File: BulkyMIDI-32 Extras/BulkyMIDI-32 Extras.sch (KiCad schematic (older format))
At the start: 64 parts, among them J1 DC IN, J10 MIDI2, J11 MIDI3, J12 SERIAL, J13 ICSP, J14 BIN/ASCII, J15 BAUD_RATE, J16 Stacked RS232 Module, J2 MIDI OUT, J3 MIDI IN, J4 Conn_Extras, J5 MIDI1, J6 RS232 Module, J7 INPUT1, J8 INPUT2, J9 OUTPUT, M1 Mounting, M2 Mounting, M3 Mounting, M4 Mounting, SW1 RESET, U1 74HCT14, U2 ATMEGA328_MCU, U3 6N138, Y1 16Mhz

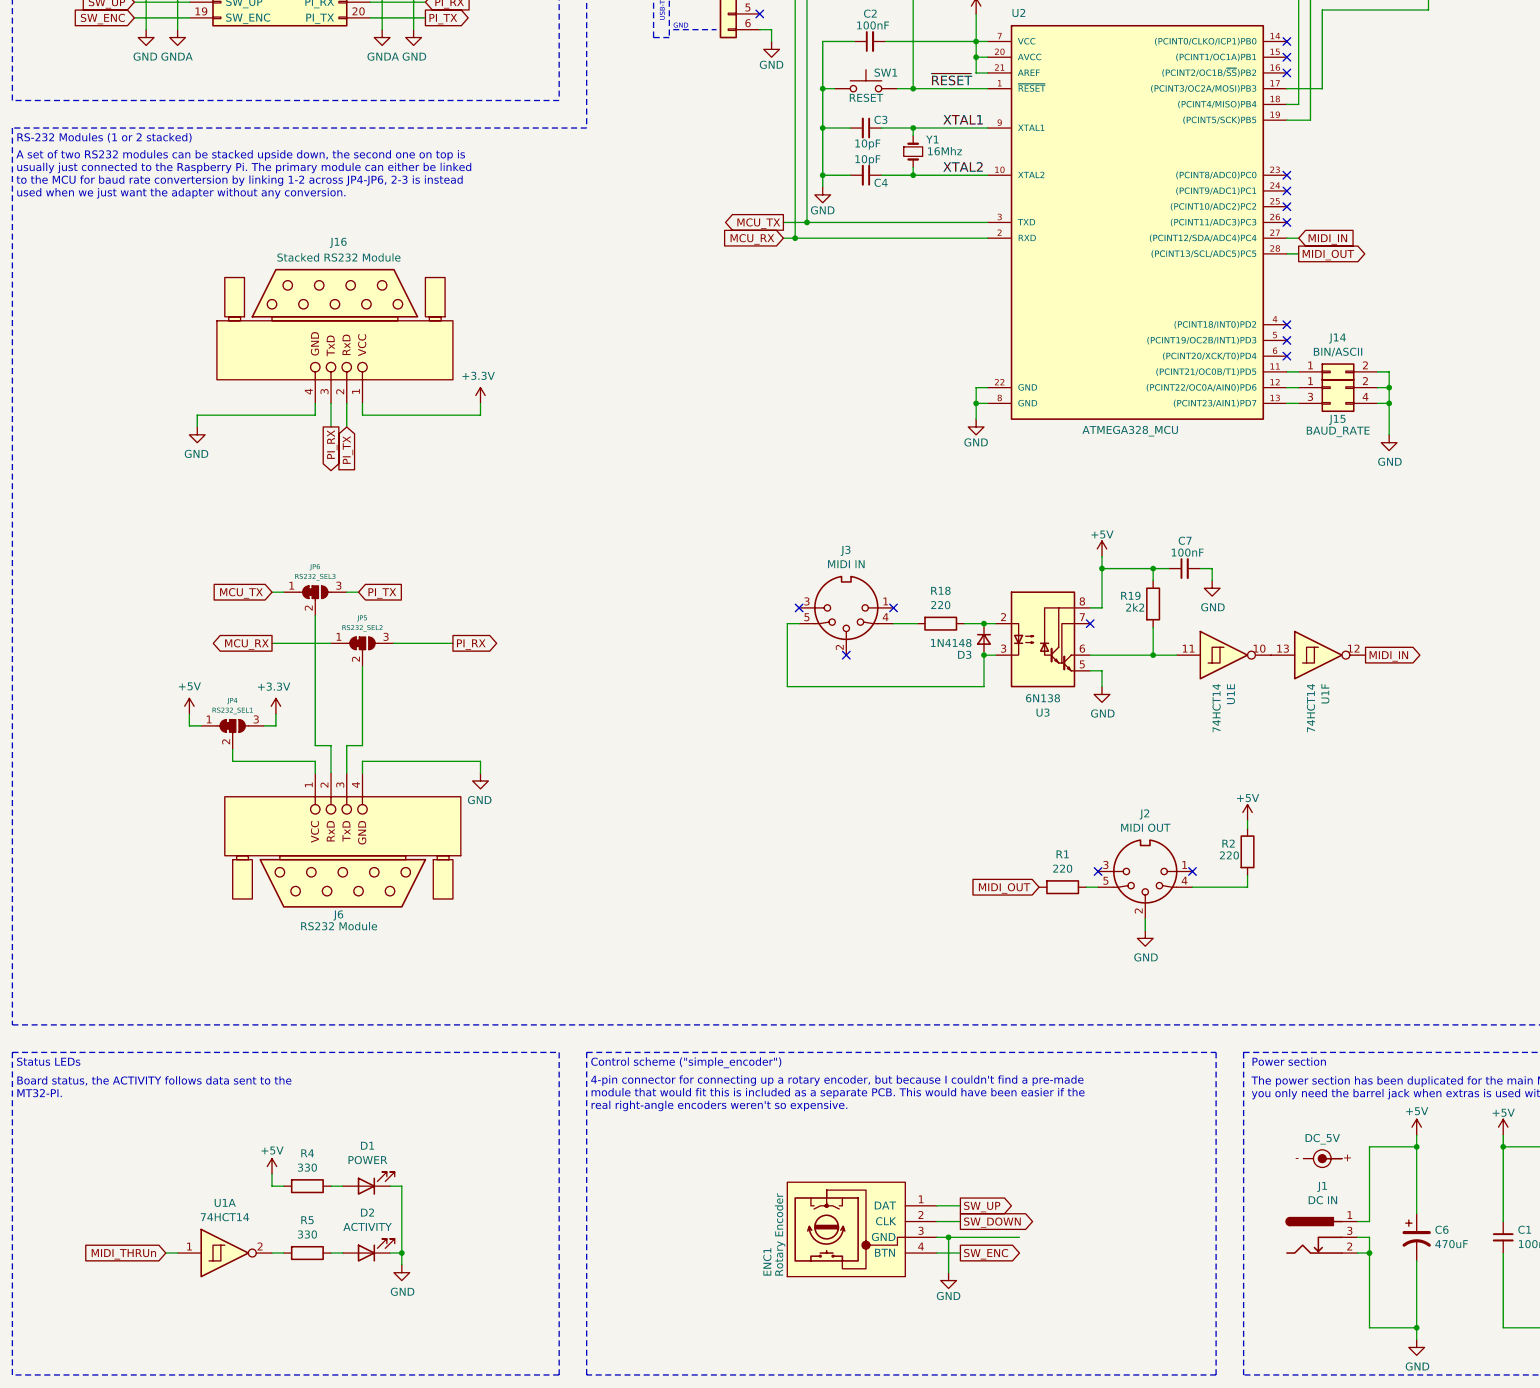
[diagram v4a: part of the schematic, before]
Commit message: Add third status LED
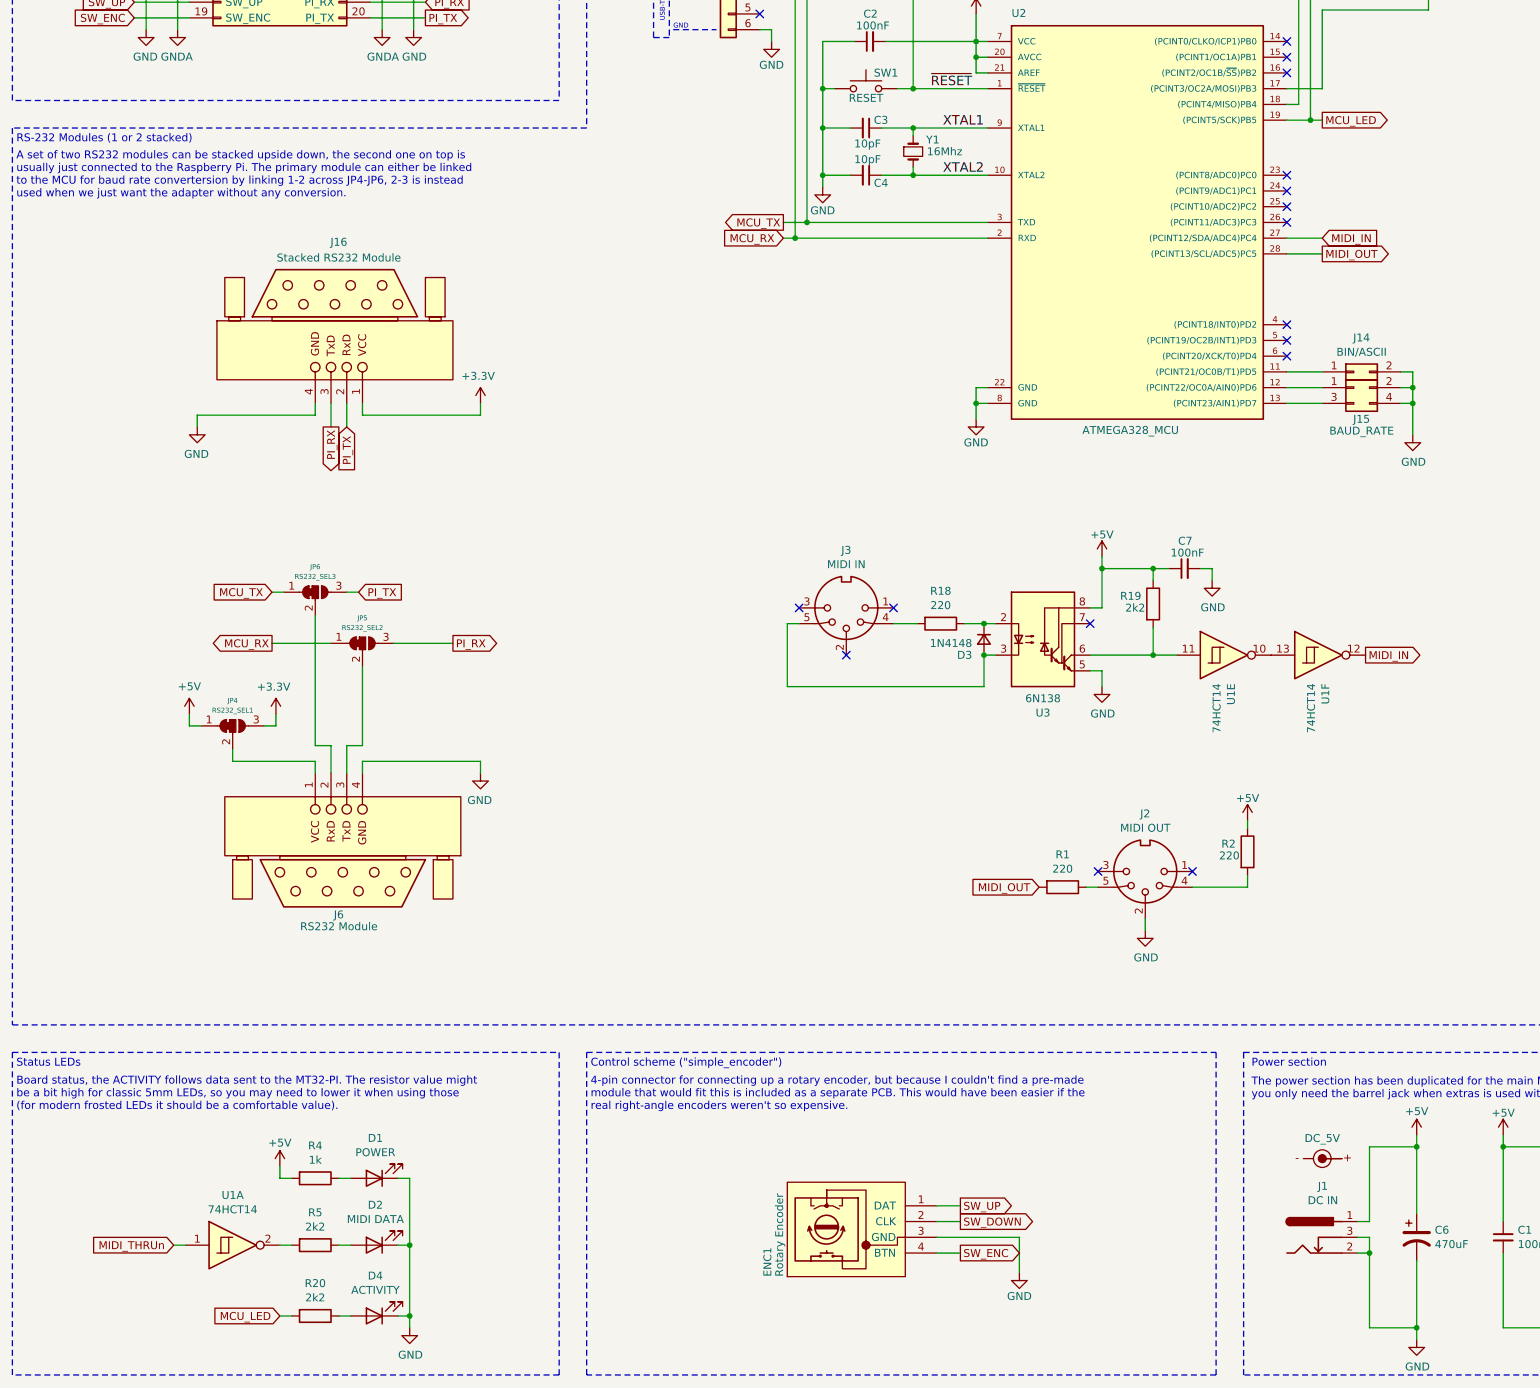
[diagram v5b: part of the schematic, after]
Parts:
- added D4: ACTIVITY, LED_THT:LED_D5.0mm_Horizontal_O1.27mm_Z3.0mm, symbol Device:LED
- added R20: 2k2, Resistor_THT:R_Axial_DIN0207_L6.3mm_D2.5mm_P10.16mm_Horizontal, symbol Device:R
- D2: value ACTIVITY -> MIDI DATA
- R4: value 330 -> 1k
- R5: value 330 -> 2k2
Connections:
- net GND: now also D4.1 (K)
- net MCU_LED: now reaches J13.3 (Pin_3), U2.19 ((PCINT5/SCK)PB5)
- net MCU_LED: now also R20.2
- new net: D4.2 (A), R20.1
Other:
- note added: "Board status, the ACTIVITY follows data sent to the MT32-PI. The resistor value might\nbe a bit high for classic 5mm LEDs, so you may need to lower it when using those\n(for modern frosted LEDs it should be a comfortable value)."
- note removed: "Board status, the ACTIVITY follows data sent to the\nMT32-PI."
- moved on the sheet: D1, D2, J14, J15, R4, R5, U1A

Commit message: Better LED naming
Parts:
- D2: value MIDI DATA -> DATA (MT-32)
- D4: value ACTIVITY -> ACTIVITY (MCU)
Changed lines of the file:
@@
 P 3300 10300
 F 0 "D2" H 3293 10045 50  0000 C CNN
-F 1 "MIDI DATA" H 3293 10136 50  0000 C CNN
+F 1 "DATA (MT-32)" H 3293 10136 50  0000 C CNN
 F 2 "LED_THT:LED_D5.0mm_Horizontal_O1.27mm_Z3.0mm" H 3300 10300 50  0001 C CNN
 F 3 "~" H 3300 10300 50  0001 C CNN
@@
 P 3300 10750
 F 0 "D4" H 3293 10495 50  0000 C CNN
-F 1 "ACTIVITY" H 3293 10586 50  0000 C CNN
+F 1 "ACTIVITY (MCU)" H 3293 10586 50  0000 C CNN
 F 2 "LED_THT:LED_D5.0mm_Horizontal_O1.27mm_Z3.0mm" H 3300 10750 50  0001 C CNN
 F 3 "~" H 3300 10750 50  0001 C CNN

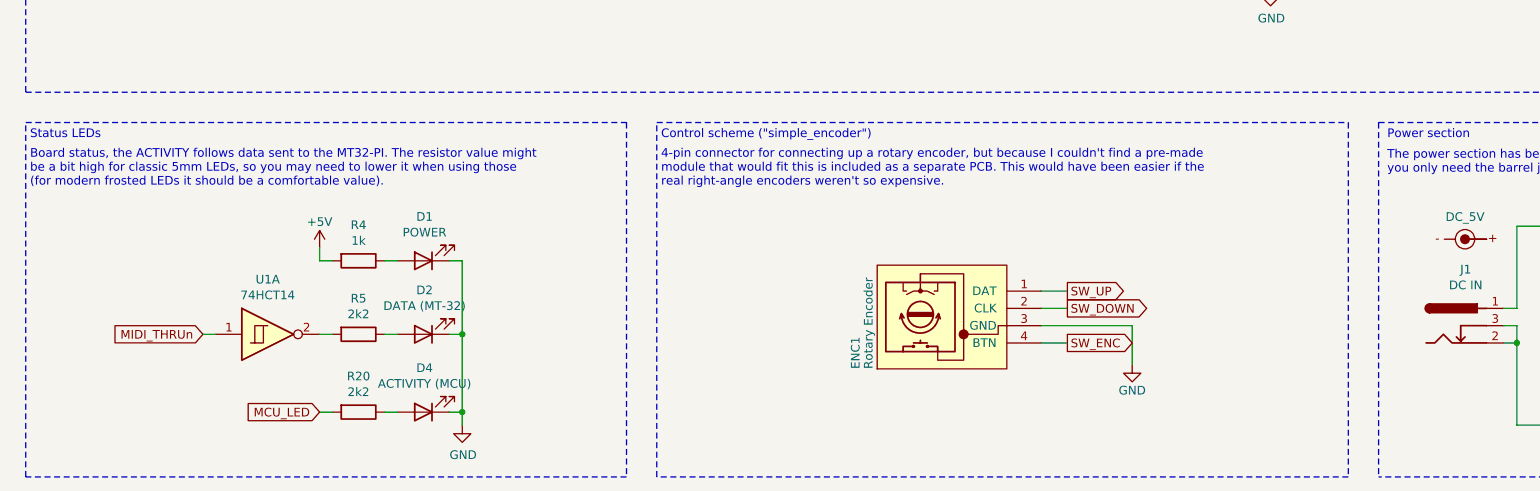
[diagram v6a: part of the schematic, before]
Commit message: Made DATA LED a bit nicer, moved rotary encoder slightly
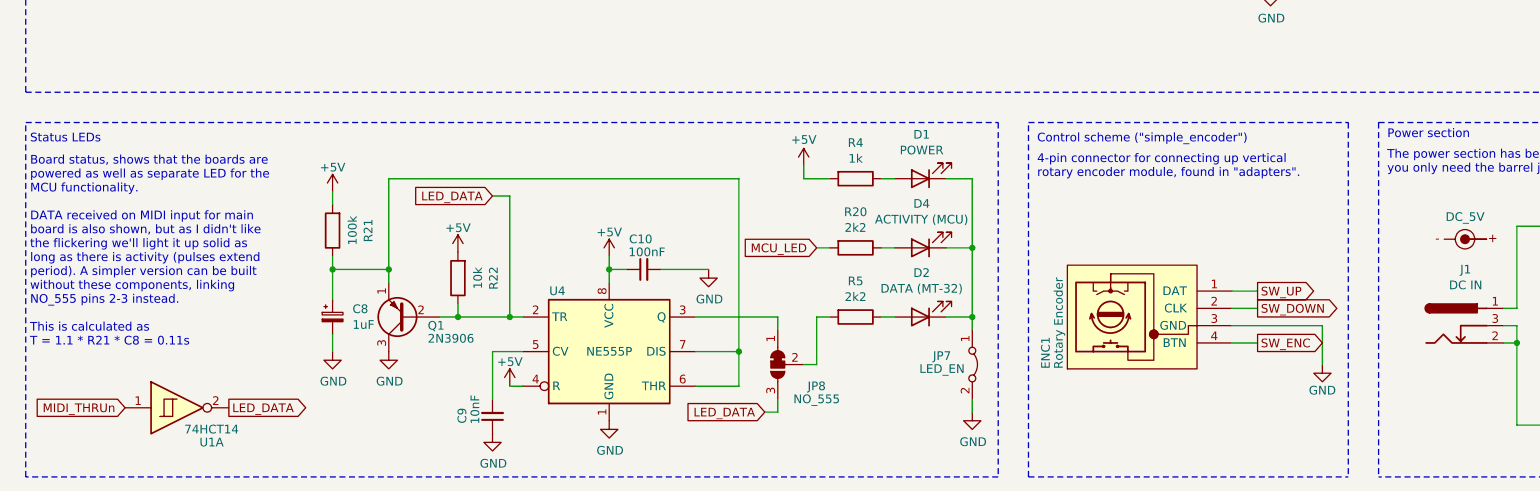
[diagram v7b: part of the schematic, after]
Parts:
- added C10: 100nF, Capacitor_THT:C_Disc_D4.7mm_W2.5mm_P5.00mm, symbol Device:C_Small
- added C8: 1uF, Capacitor_THT:CP_Radial_D5.0mm_P2.00mm, symbol Device:CP_Small
- added C9: 10nF, Capacitor_THT:C_Disc_D4.7mm_W2.5mm_P5.00mm, symbol Device:C_Small
- added JP7: LED_EN, Connector_PinHeader_2.54mm:PinHeader_1x02_P2.54mm_Vertical, symbol Jumper:Jumper_2_Bridged
- added JP8: NO_555, Jumper:SolderJumper-3_P1.3mm_Open_Pad1.0x1.5mm, symbol Jumper:SolderJumper_3_Bridged12
- added Q1: 2N3906, Package_TO_SOT_THT:TO-92_Inline_Wide, symbol Transistor_BJT:2N3906
- added R21: 100k, Resistor_THT:R_Axial_DIN0207_L6.3mm_D2.5mm_P10.16mm_Horizontal, symbol Device:R
- added R22: 10k, Resistor_THT:R_Axial_DIN0207_L6.3mm_D2.5mm_P10.16mm_Horizontal, symbol Device:R
- added U4: NE555P, Package_DIP:DIP-8_W7.62mm_Socket_LongPads, symbol Timer:NE555P
- SW1: footprint Button_Switch_THT:SW_PUSH_6mm -> Button_Switch_THT:SW_Tactile_SPST_Angled_PTS645Vx39-2LFS
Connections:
- net +5V: now also C10.1, R21.2, R22.2, U4.4 (R), U4.8 (VCC)
- net GND: now also C10.2, C8.2, C9.1, JP7.2 (B), Q1.3 (C), U4.1 (GND); no longer D1.1 (K), D2.1 (K), D4.1 (K)
- net at R5.2: now also JP8.2 (C); no longer U1.2
- new net: D1.1 (K), D2.1 (K), D4.1 (K), JP7.1 (A)
- new net: JP8.1 (A), U4.3 (Q)
- new net: C9.2, U4.5 (CV)
- new net: C8.1, Q1.1 (E), R21.1, U4.6 (THR), U4.7 (DIS)
- new net LED_DATA: JP8.3 (B), Q1.2 (B), R22.1, U1.2, U4.2 (TR)
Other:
- note added: "4-pin connector for connecting up vertical\nrotary encoder module, found in "adapters"."
- note added: "Board status, shows that the boards are\npowered as well as separate LED for the\nMCU functionality.\n\nDATA received on MIDI input for main\nboard is also shown, but as I didn't like\nthe flickering we'll light it up solid as\nlong as there is activity (pulses extend\nperiod). A simpler version can be built\nwithout these components, linking\nNO_555 pins 2-3 instead.\n\nThis is calculated as\nT 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"
- note removed: "4-pin connector for connecting up a rotary encoder, but because I couldn't find a pre-made\nmodule that would fit this is included as a separate PCB. This would have been easier if the\nreal right-angle encoders weren't so expensive."
- note removed: "Board status, the ACTIVITY follows data sent to the MT32-PI. The resistor value might\nbe a bit high for classic 5mm LEDs, so you may need to lower it when using those\n(for modern frosted LEDs it should be a comfortable value)."
- moved on the sheet: D1, D2, D4, ENC1, R20, R4, R5, U1A

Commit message: Module FP1 sketched out
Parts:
- removed D1: POWER, LED_THT:LED_D5.0mm_Horizontal_O1.27mm_Z3.0mm, symbol Device:LED
- removed ENC1: Rotary Encoder, BulkyMIDI-32:Vertical_Rotary_Encoder, symbol BulkyMIDI:Vertical_Rotary_Encoder
- removed R4: 1k, Resistor_THT:R_Axial_DIN0207_L6.3mm_D2.5mm_P10.16mm_Horizontal, symbol Device:R
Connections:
- net SW_DOWN: no longer names the net of J4.15 (SW_DOWN)
- net SW_ENC: no longer names the net of J4.19 (SW_ENC)
- net SW_UP: no longer names the net of J4.17 (SW_UP)
- no-connect marks 30 -> 33
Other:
- note removed: "4-pin connector for connecting up vertical\nrotary encoder module, found in "adapters"."
- note removed: "Control scheme ("simple_encoder")"
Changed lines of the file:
@@
 Title "BulkyMIDI-32 Extras"
 Date ""
-Rev "B"
+Rev "D"
 Comp ""
 Comment1 ""
@@
 RS-232 Baud rate converter
 $Comp
-L BulkyMIDI:Vertical_Rotary_Encoder ENC1
-U 1 1 62EDD8FE
-P 7325 10200
-F 0 "ENC1" H 7025 10625 50  0000 L CNN
-F 1 "Rotary Encoder" H 7025 10550 50  0000 L CNN
-F 2 "BulkyMIDI-32:Vertical_Rotary_Encoder" H 7475 10090 50  0001 C CNN
-F 3 "~" H 7325 9990 50  0001 C CNN
-	1    7325 10200
-	0    -1   -1   0
-$EndComp
-Text GLabel 8125 10350 2    50   Output ~ 0
-SW_ENC
-Text GLabel 8125 10050 2    50   Output ~ 0
-SW_UP
-Text GLabel 8125 10150 2    50   Output ~ 0
-SW_DOWN
-$Comp
-L power:GND #PWR06
-U 1 1 62F29FB2
-P 8500 10475
-F 0 "#PWR06" H 8500 10225 50  0001 C CNN
-F 1 "GND" H 8500 10325 50  0000 C CNN
-F 2 "" H 8500 10475 50  0001 C CNN
-F 3 "" H 8500 10475 50  0001 C CNN
-	1    8500 10475
-	-1   0    0    -1
-$EndComp
-$Comp
 L Connector:DIN-5_180degree J3
 U 1 1 5F99CA21
@@
 Wire Notes Line
 	15325 5400 11300 5400
-Text Notes 6850 9200 0    50   ~ 0
-Control scheme ("simple_encoder")
 Text Notes 8875 9175 0    50   ~ 0
 Power section
-Text Notes 6850 9400 0    50   ~ 0
-4-pin connector for connecting up vertical\nrotary encoder module, found in "adapters".
 $Comp
 L Device:R_POT_Dual RV1
@@
 Wire Wire Line
 	3625 2500 3275 2500
-Text GLabel 1775 2500 0    50   Input ~ 0
-SW_ENC
-Text GLabel 1775 2400 0    50   Input ~ 0
-SW_UP
-Text GLabel 1775 2300 0    50   Input ~ 0
-SW_DOWN
-Wire Wire Line
-	1775 2300 2125 2300
-Wire Wire Line
-	2125 2400 1775 2400
-Wire Wire Line
-	1775 2500 2125 2500
 $Comp
 L Device:LED D2
@@
 	13475 7175 13550 7175
 $Comp
-L Device:LED D1
-U 1 1 62716DB3
-P 6175 9400
-F 0 "D1" H 6168 9145 50  0000 C CNN
-F 1 "POWER" H 6168 9236 50  0000 C CNN
-F 2 "LED_THT:LED_D5.0mm_Horizontal_O1.27mm_Z3.0mm" H 6175 9400 50  0001 C CNN
-F 3 "~" H 6175 9400 50  0001 C CNN
-	1    6175 9400
-	-1   0    0    1
-$EndComp
-$Comp
 L Device:R R5
 U 1 1 62729C3C
@@
 Wire Wire Line
 	5950 10200 6025 10200
-Wire Wire Line
-	6025 9400 5950 9400
-$Comp
-L Device:R R4
-U 1 1 6276F7E0
-P 5800 9400
-F 0 "R4" V 5593 9400 50  0000 C CNN
-F 1 "1k" V 5684 9400 50  0000 C CNN
-F 2 "Resistor_THT:R_Axial_DIN0207_L6.3mm_D2.5mm_P10.16mm_Horizontal" V 5730 9400 50  0001 C CNN
-F 3 "~" H 5800 9400 50  0001 C CNN
-	1    5800 9400
-	0    1    1    0
-$EndComp
-$Comp
-L power:+5V #PWR09
-U 1 1 62779CD7
-P 5500 9325
-F 0 "#PWR09" H 5500 9175 50  0001 C CNN
-F 1 "+5V" H 5500 9475 50  0000 C CNN
-F 2 "" H 5500 9325 50  0001 C CNN
-F 3 "" H 5500 9325 50  0001 C CNN
-	1    5500 9325
-	1    0    0    -1
-$EndComp
-Wire Wire Line
-	5500 9325 5500 9400
 Text Notes 1025 9200 0    50   ~ 0
 Status LEDs
@@
 	6150 2650 6150 2950
 Connection ~ 6150 2950
-Wire Notes Line
-	8650 9075 8650 11125
-Wire Notes Line
-	6800 11125 6800 9075
-Wire Wire Line
-	8500 10250 8500 10475
-Wire Wire Line
-	8125 10350 7975 10350
-Wire Wire Line
-	7975 10150 8125 10150
-Wire Wire Line
-	7975 10050 8125 10050
 Wire Notes Line
 	11125 8900 11125 575
@@
 Wire Wire Line
 	5650 9800 5575 9800
-Wire Wire Line
-	7975 10250 8500 10250
 $Comp
 L Timer:NE555P U4
@@
 	6325 10200 6475 10200
 Connection ~ 6475 10200
-Wire Wire Line
-	6325 9400 6475 9400
-Wire Notes Line
-	6800 11125 8650 11125
-Wire Notes Line
-	6800 9075 8650 9075
 Wire Notes Line
 	1000 9075 6625 9075
@@
 	4875 10400 5125 10400
 Wire Wire Line
-	5500 9400 5650 9400
-Wire Wire Line
 	6475 9800 6475 10200
 Wire Wire Line
 	6475 10200 6475 10275
-Wire Wire Line
-	6475 9400 6475 9800
-Connection ~ 6475 9800
 Wire Wire Line
 	6475 10750 6475 10675
@@
 Wire Wire Line
 	3700 10400 3875 10400
+NoConn ~ 2125 2300
+NoConn ~ 2125 2400
+NoConn ~ 2125 2500
 $EndSCHEMATC
